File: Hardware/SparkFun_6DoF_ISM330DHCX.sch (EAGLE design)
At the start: 31 parts, among them J1 QWIIC_RIGHT_ANGLE, J2 QWIIC_RIGHT_ANGLE, U1 LSM6DS0

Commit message: Adds ISM330DHCX part
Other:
- note added: "v01"
- note removed: "Revised by: Elias Santistevan"
- note removed: "v10"
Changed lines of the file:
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@@
 MODE3:  AUX SPI mode
    I2C and SPI access (Multi-read)   </text>
-<text x="148.844" y="6.858" size="2.54" layer="94" font="vector">Revised by: Elias Santistevan</text>
 <wire x1="0" y1="86.36" x2="114.3" y2="86.36" width="0.2032" layer="97" style="longdash"/>
 <wire x1="114.3" y1="86.36" x2="248.92" y2="86.36" width="0.2032" layer="97" style="longdash"/>
@@
 <text x="45.466" y="150.114" size="1.27" layer="97" font="vector">VDD Range: 1.71V - 3.6V
 VDDIO Range: 1.62V - 3.6V</text>
-<text x="238.76" y="7.62" size="2.54" layer="94" font="vector">v10</text>
+<text x="238.76" y="7.62" size="2.54" layer="94" font="vector">v01</text>
 <text x="215.646" y="141.986" size="1.778" layer="97" font="vector">0x6B (Default)
 0x6A
@@
 <instance part="FRAME1" gate="G$1" x="0" y="0" smashed="yes"/>
 <instance part="FRAME1" gate="V" x="147.32" y="0" smashed="yes">
-<attribute name="DESIGNER" x="167.132" y="11.43" size="2.54" layer="94" font="vector"/>
 <attribute name="LAST_DATE_TIME" x="160.02" y="1.27" size="2.54" layer="94" font="vector"/>
 <attribute name="SHEET" x="233.68" y="1.27" size="2.54" layer="94" font="vector"/>

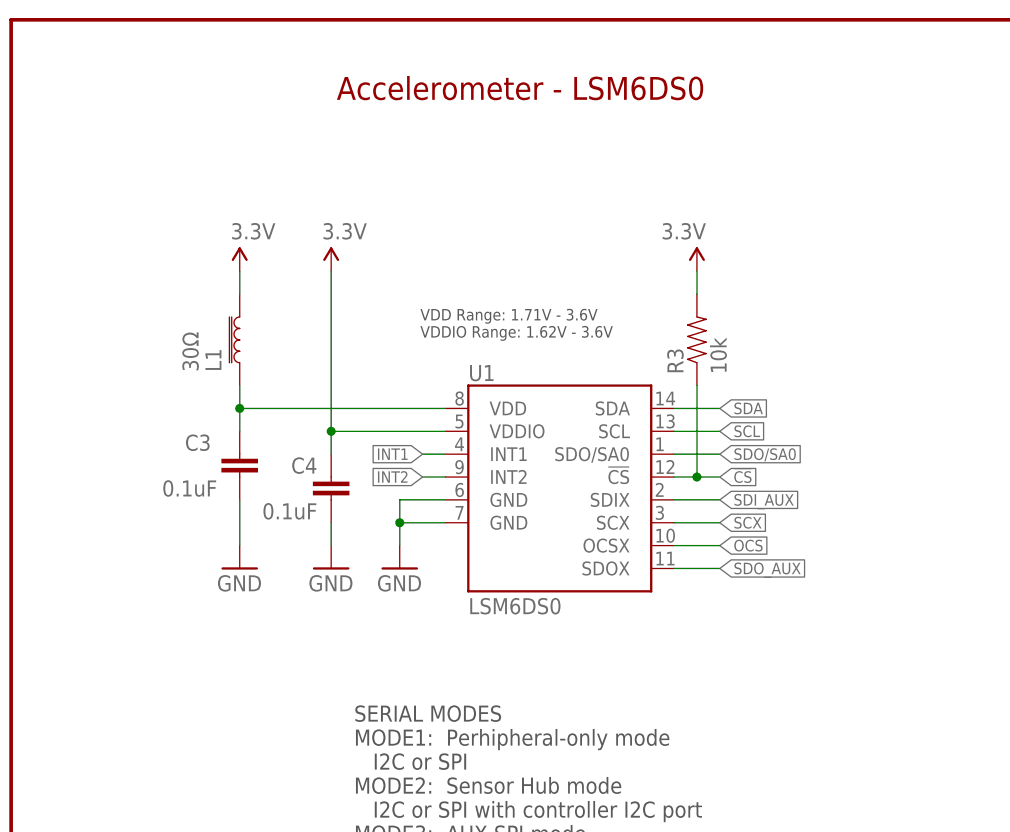
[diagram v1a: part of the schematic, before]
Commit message: Fixes IC name
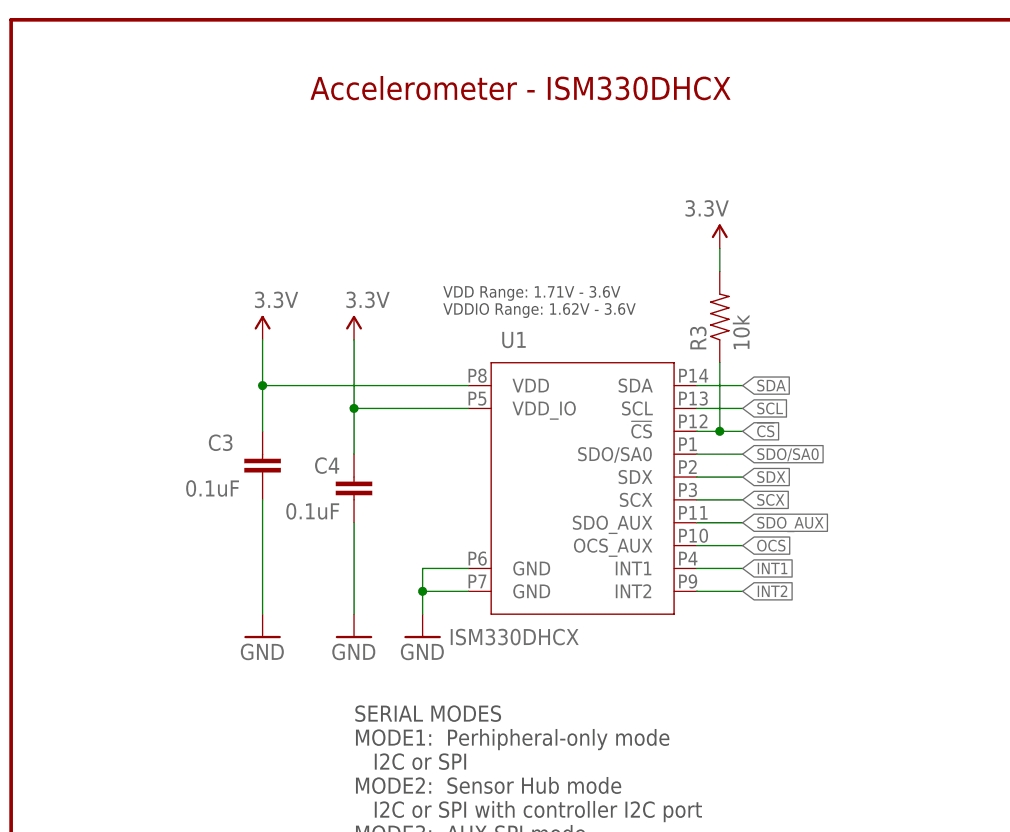
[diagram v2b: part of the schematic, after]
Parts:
- removed L1: 30Ω, SparkFun-Coils:FERRITE_BEAD-0603-30OHM-100MHZ
- U1: value LSM6DS0 -> ISM330DHCX; device temp:LSM6DS0 -> ISM330DHCX:ISM330DHCX
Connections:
- removed net VDD: C3.1, L1.2, U1.VDD
- new net N$4: C3.1, U1.VDD
- new net SDX: U1.SDX
- net 3.3V: now also U1.VDD_IO; no longer L1.1, U1.VDDIO
- net OCS: now also U1.OCS_AUX; no longer U1.OCSX
- net SDI_AUX: no longer U1.SDIX
- net SDO_AUX: now also U1.SDO_AUX; no longer U1.SDOX
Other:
- note added: "Accelerometer - ISM330DHCX"
- note removed: "Accelerometer - LSM6DS0"
- moved on the sheet: C3, C4, R3, U1

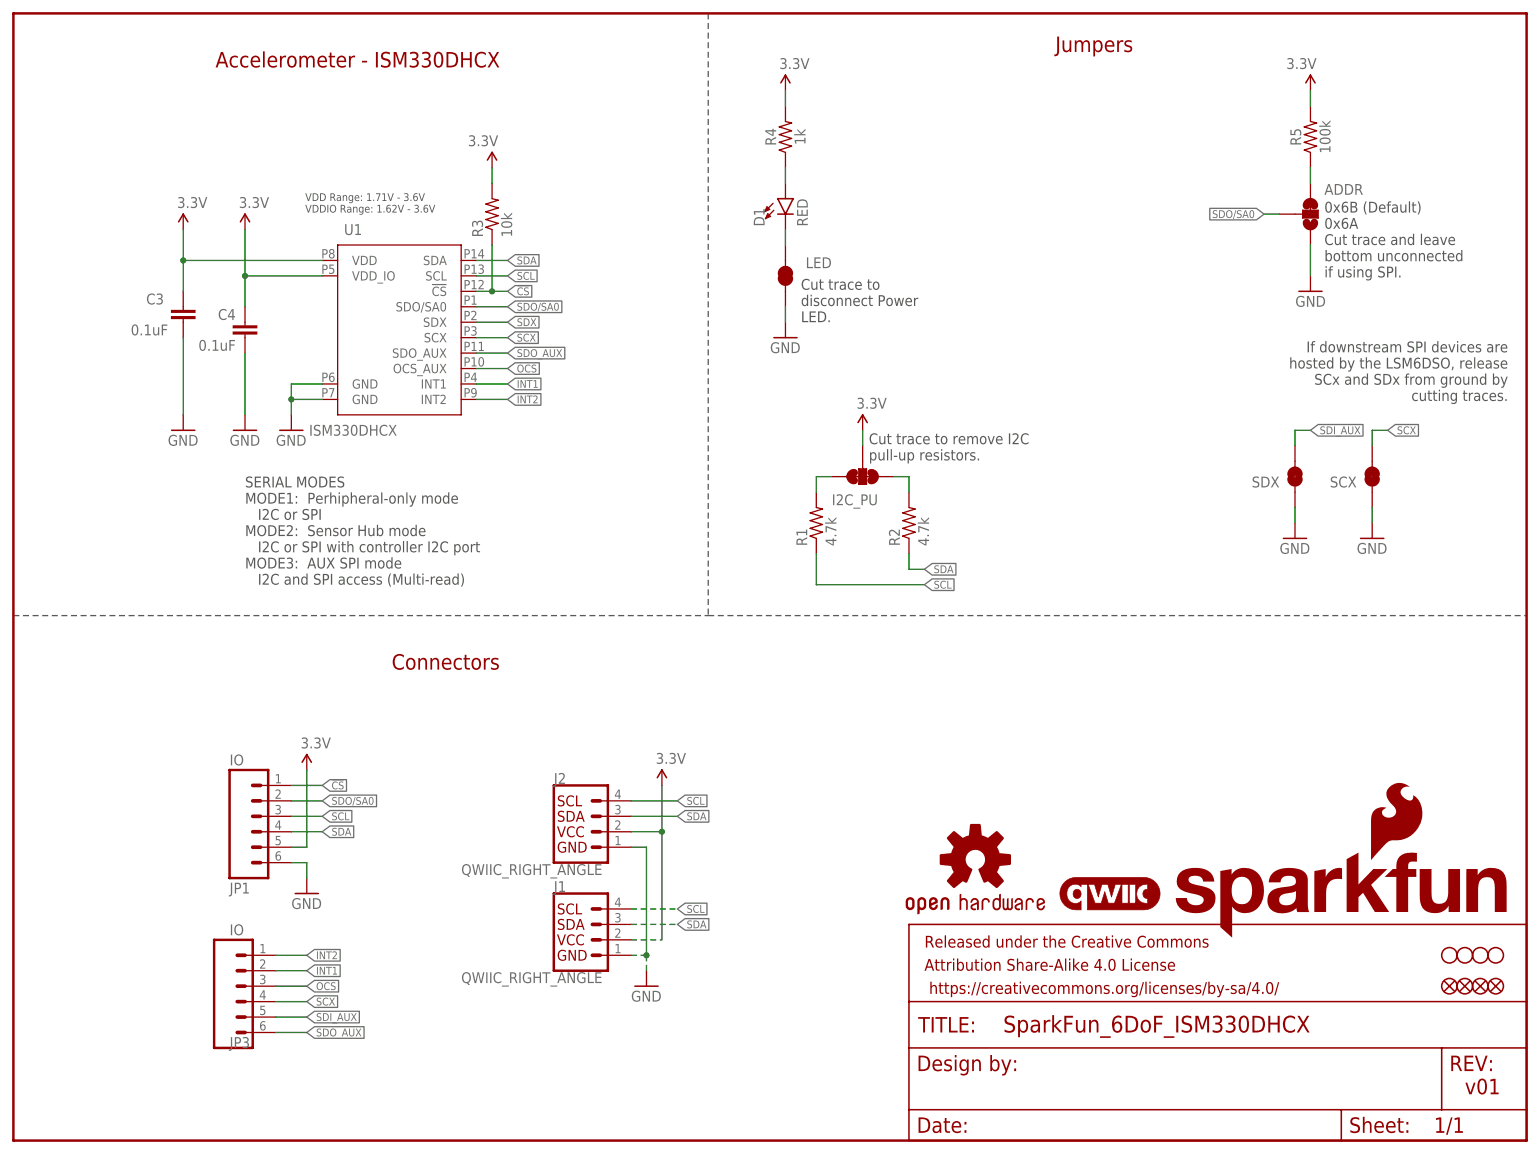
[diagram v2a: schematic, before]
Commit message: Updates notes in schematic (schematic done)
* Adds 10k to ground to address selection just in case someone bridges the entire three way jumper
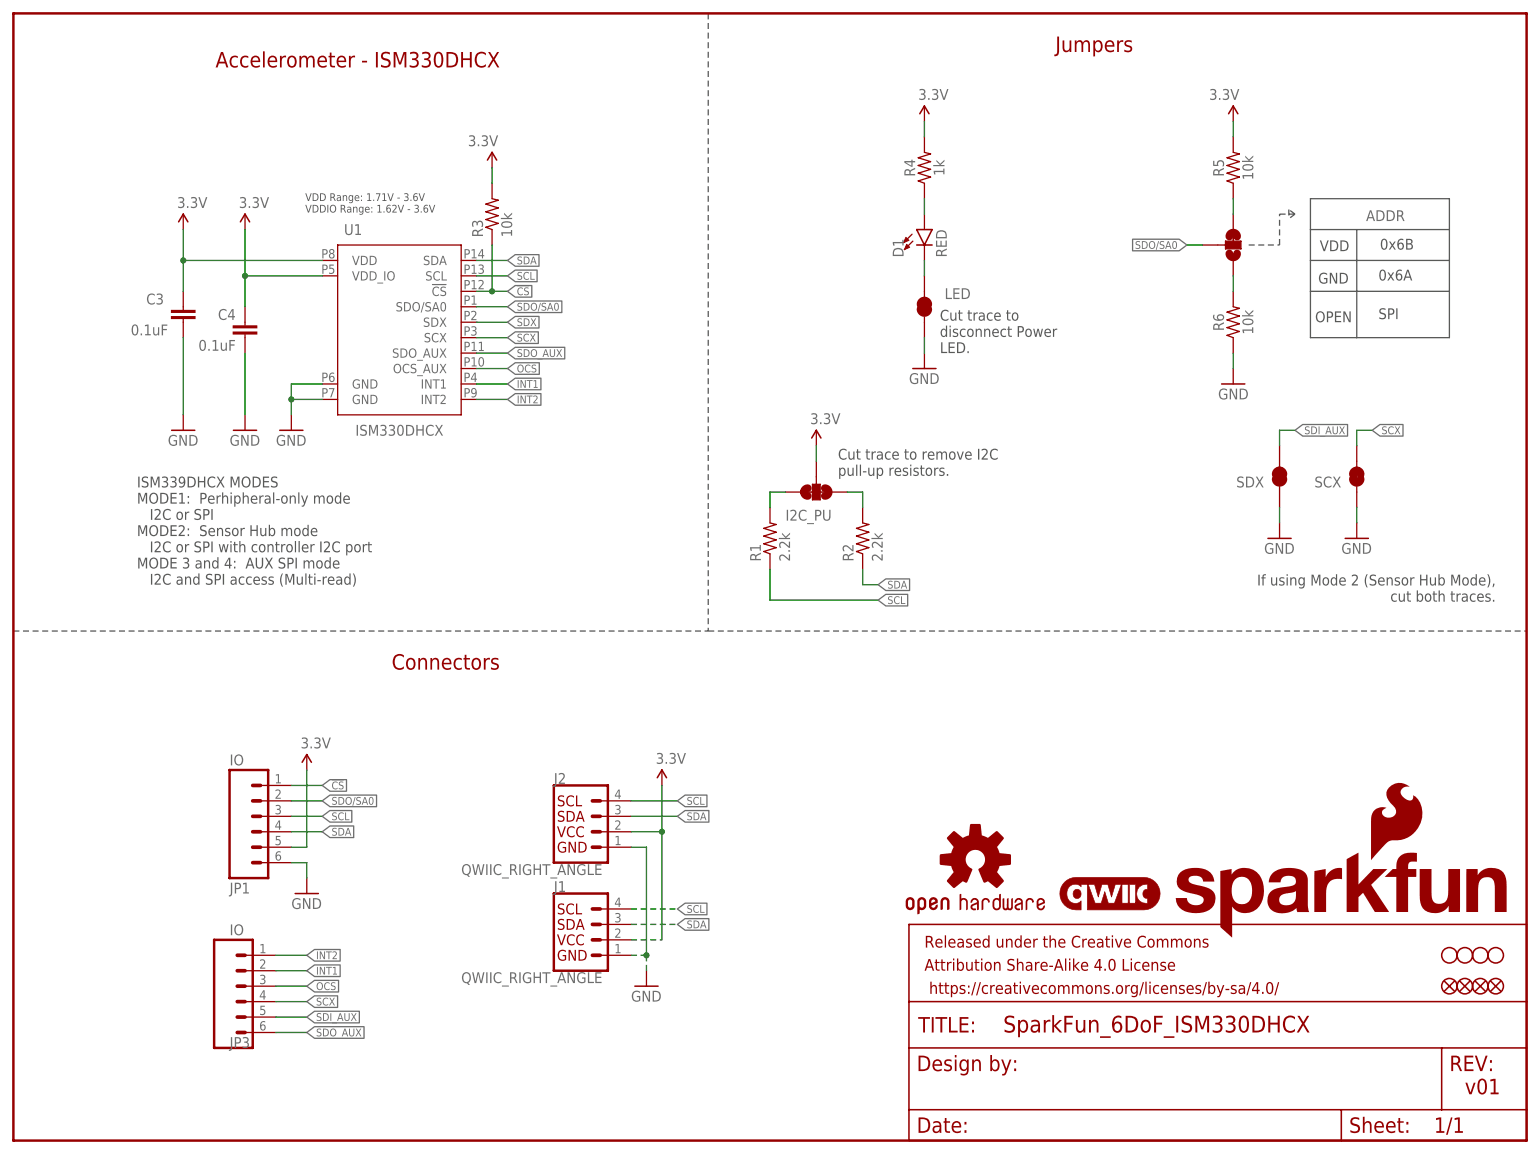
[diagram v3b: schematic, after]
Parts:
- added R6: 10k, SparkFun-Resistors:10KOHM-0603-1/10W-1%
- R1, R2: value 4.7k -> 2.2k; device SparkFun-Resistors:4.7KOHM-0603-1/10W-1% -> SparkFun-Resistors:2.2KOHM-0603-1/10W-1%
- R5: value 100k -> 10k; device SparkFun-Resistors:100KOHM-0603-1/10W-1% -> SparkFun-Resistors:10KOHM-0603-1/10W-1%
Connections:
- new net N$7: ADDR.1, R6.2
- net GND: now also R6.1; no longer ADDR.1
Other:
- note added: "0x6A"
- note added: "0x6B"
- note added: "GND"
- note added: "ISM339DHCX MODES MODE1: Perhipheral-only mode I2C or SPI MODE2: Sensor Hub mode I2C or SPI with controller I2C port MODE 3 and 4: AUX SPI mode I2C and SPI access (Multi-read)"
- note added: "If using Mode 2 (Sensor Hub Mode), cut both traces."
- note added: "OPEN"
- note added: "SPI"
- note added: "VDD"
- note removed: "0x6B (Default) 0x6A Cut trace and leave bottom unconnected if using SPI."
- note removed: "If downstream SPI devices are hosted by the LSM6DSO, release SCx and SDx from ground by cutting traces."
- note removed: "SERIAL MODES MODE1: Perhipheral-only mode I2C or SPI MODE2: Sensor Hub mode I2C or SPI with controller I2C port MODE3: AUX SPI mode I2C and SPI access (Multi-read)"
- moved on the sheet: ADDR, D1, I2C_PU, LED, R1, R2, R4, R5, SCX, SDX
